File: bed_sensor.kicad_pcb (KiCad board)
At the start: 2 copper layers, 41 x 36 mm, 32 parts, among them J1 Conn_01x02, J2 Conn_01x06, J3 ISP, J4 Conn_01x02, Q1 2N2219, SW1 SW_SPST, U1 MIC5205-3.3, U2 MPU-9250, U5 CFAH0802D-YYH-JP, U6 ATMEGA328-AU, Y1 Crystal_GND2

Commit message: updated pcb layout
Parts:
- added C6: .1uF, Capacitor_SMD:C_0603_1608Metric, F.Cu at (147.4, 108.6)
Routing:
- net +3V3: track 144.0 -> 145.3 mm
- net GND: track 66.8 -> 68.2 mm, vias 12 -> 13
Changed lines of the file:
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@@
     (thickness 1.6)
     (drawings 12)
-    (tracks 435)
+    (tracks 442)
     (zones 0)
-    (modules 32)
+    (modules 33)
     (nets 32)
   )
@@
       (outputformat 1)
       (mirror false)
-      (drillshape 1)
+      (drillshape 0)
       (scaleselection 1)
-      (outputdirectory ""))
+      (outputdirectory ../../Downloads/bed_sensor_pcb/))
   )
   (net 0 "")
@@
     )
   )
+  (module Capacitor_SMD:C_0603_1608Metric (layer F.Cu)
+    (at 147.375001 108.63 180)
+    (descr "Capacitor SMD 0603 (1608 Metric), square (rectangular) end terminal, IPC_7351 nominal, (Body size source: http://www.tortai-tech.com/upload/download/2011102023233369053.pdf), generated with kicad-footprint-generator")
+    (tags capacitor)
+    (attr smd)
+    (fp_text reference C6 (at 0 -1.45 180) (layer F.SilkS)
+      (effects (font (size 1 1) (thickness 0.15)))
+    )
+    (fp_text value .1uF (at 0 1.45 180) (layer F.Fab)
+      (effects (font (size 1 1) (thickness 0.15)))
+    )
+    (fp_line (start -0.8 0.4) (end -0.8 -0.4) (layer F.Fab) (width 0.1))
+    (fp_line (start -0.8 -0.4) (end 0.8 -0.4) (layer F.Fab) (width 0.1))
+    (fp_line (start 0.8 -0.4) (end 0.8 0.4) (layer F.Fab) (width 0.1))
+    (fp_line (start 0.8 0.4) (end -0.8 0.4) (layer F.Fab) (width 0.1))
+    (fp_line (start -1.46 0.75) (end -1.46 -0.75) (layer F.CrtYd) (width 0.05))
+    (fp_line (start -1.46 -0.75) (end 1.46 -0.75) (layer F.CrtYd) (width 0.05))
+    (fp_line (start 1.46 -0.75) (end 1.46 0.75) (layer F.CrtYd) (width 0.05))
+    (fp_line (start 1.46 0.75) (end -1.46 0.75) (layer F.CrtYd) (width 0.05))
+    (fp_text user %R (at 0 0 180) (layer F.Fab)
+      (effects (font (size 0.4 0.4) (thickness 0.06)))
+    )
+    (pad 1 smd rect (at -0.8 0 180) (size 0.82 1) (layers F.Cu F.Paste F.Mask)
+      (net 2 GND))
+    (pad 2 smd rect (at 0.8 0 180) (size 0.82 1) (layers F.Cu F.Paste F.Mask)
+      (net 4 +3V3))
+    (model ${KISYS3DMOD}/Capacitor_SMD.3dshapes/C_0603_1608Metric.wrl
+      (at (xyz 0 0 0))
+      (scale (xyz 1 1 1))
+      (rotate (xyz 0 0 0))
+    )
+  )
   (gr_arc (start 117.749001 120.976) (end 116.225001 120.976) (angle -90) (layer Edge.Cuts) (width 0.15))
   (gr_arc (start 155.701001 120.976) (end 155.701001 122.5) (angle -90) (layer Edge.Cuts) (width 0.15))
@@
   (segment (start 142.693529 94.061472) (end 143.855001 92.9) (width 0.25) (layer F.Cu) (net 2))
   (segment (start 142.693529 94.458528) (end 142.693529 94.061472) (width 0.25) (layer F.Cu) (net 2))
+  (via (at 149.475001 108.59) (size 0.8) (drill 0.4) (layers F.Cu B.Cu) (net 2))
+  (segment (start 148.175001 108.63) (end 149.435001 108.63) (width 0.25) (layer F.Cu) (net 2))
+  (segment (start 149.435001 108.63) (end 149.475001 108.59) (width 0.25) (layer F.Cu) (net 2))
   (segment (start 150.559081 103.74808) (end 147.848001 101.037) (width 0.3) (layer F.Cu) (net 3) (status 30))
   (segment (start 150.559081 103.97816) (end 150.559081 103.74808) (width 0.3) (layer F.Cu) (net 3) (status 30))
@@
   (segment (start 145.485002 109.460001) (end 144.105001 109.460001) (width 0.2) (layer F.Cu) (net 4))
   (segment (start 145.485002 107.199999) (end 146.225001 106.46) (width 0.3) (layer F.Cu) (net 4))
-  (segment (start 145.485002 109.460001) (end 145.485002 107.199999) (width 0.3) (layer F.Cu) (net 4))
   (segment (start 145.685001 109.66) (end 145.485002 109.460001) (width 0.3) (layer F.Cu) (net 4))
   (segment (start 141.935001 109.98) (end 141.935001 111.8) (width 0.2) (layer F.Cu) (net 4))
@@
   (segment (start 145.393972 96.646029) (end 145.250224 96.646029) (width 0.3) (layer F.Cu) (net 4))
   (segment (start 142.236199 102.838802) (end 142.236199 99.660054) (width 0.3) (layer F.Cu) (net 4))
+  (segment (start 145.485002 109.009999) (end 145.865001 108.63) (width 0.3) (layer F.Cu) (net 4))
+  (segment (start 145.485002 109.1) (end 145.485002 109.009999) (width 0.3) (layer F.Cu) (net 4))
+  (segment (start 145.485002 109.460001) (end 145.485002 109.1) (width 0.3) (layer F.Cu) (net 4))
+  (segment (start 145.865001 108.63) (end 146.575001 108.63) (width 0.3) (layer F.Cu) (net 4))
+  (segment (start 145.485002 109.1) (end 145.485002 107.199999) (width 0.3) (layer F.Cu) (net 4))
   (segment (start 142.805001 109.91) (end 142.805001 110.9) (width 0.2) (layer F.Cu) (net 5))
   (segment (start 143.305001 111.4) (end 143.755001 111.4) (width 0.2) (layer F.Cu) (net 5))
@@
     (polygon
       (pts
-        (xy 111.975001 82.64) (xy 112.905001 135.17) (xy 161.375001 130.53) (xy 160.145001 82.35)
+        (xy 111.975001 82.64) (xy 112.905001 135.17) (xy 161.375001 130.53) (xy 159.515001 81.38)
       )
     )

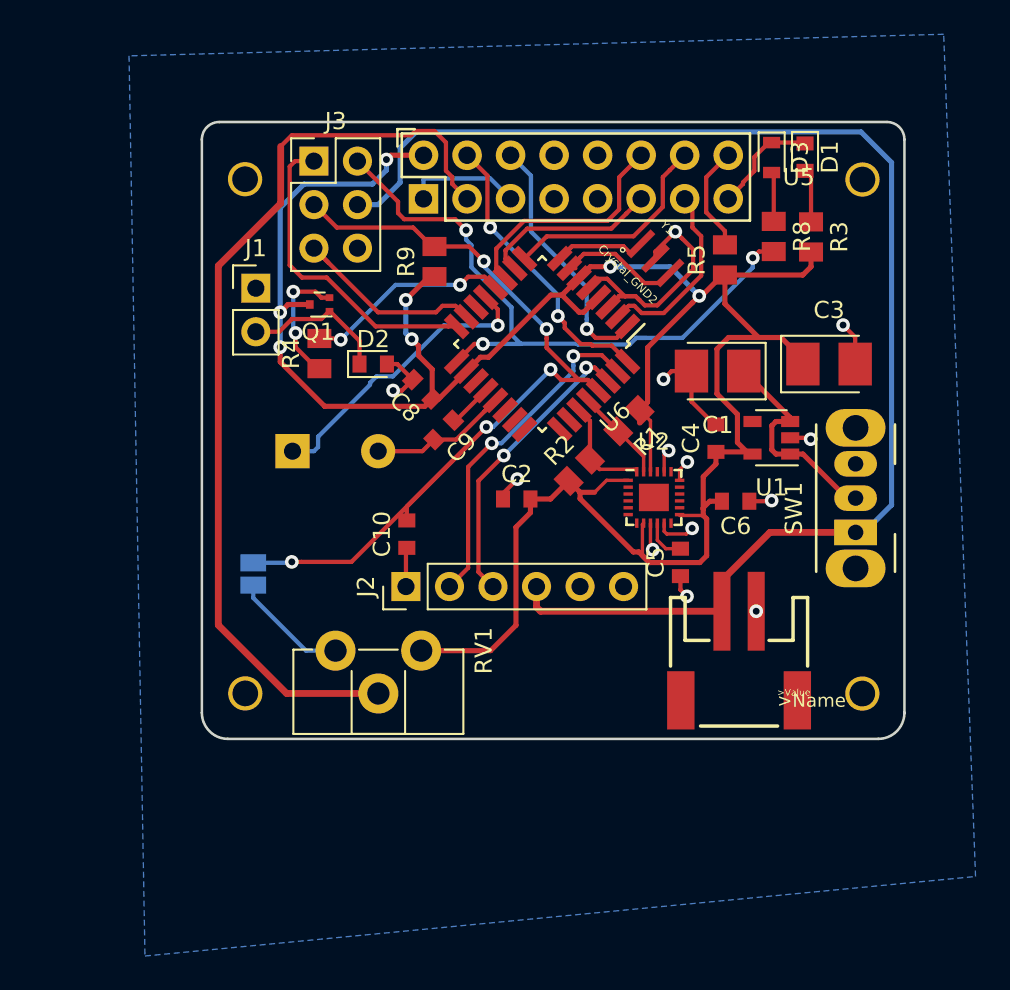
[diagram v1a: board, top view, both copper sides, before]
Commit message: corrected pinout for NHD display
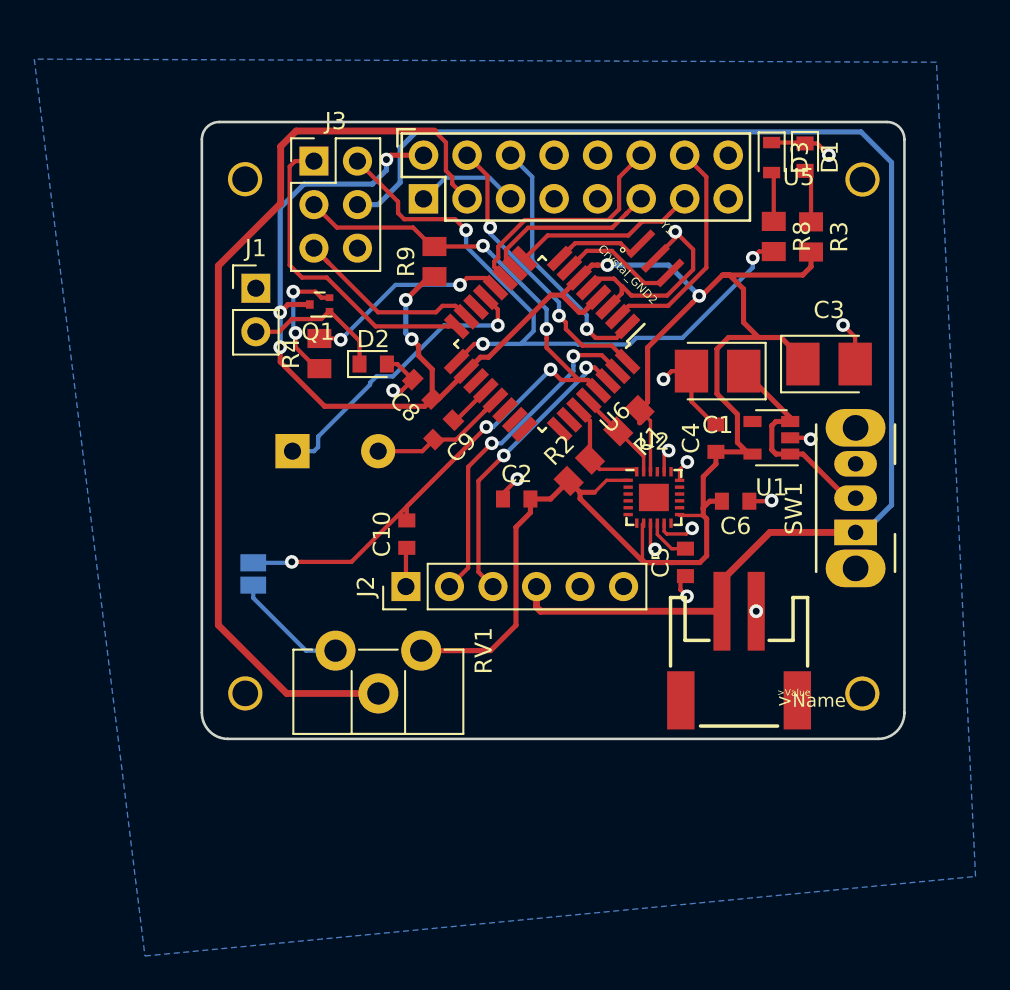
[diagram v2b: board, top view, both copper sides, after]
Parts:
- removed R5: 220, Resistor_SMD:R_0805_2012Metric
- moved C5 0.29 mm to (144.4, 112.2)
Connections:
- U1 pad 4: (no net) -> Net-(U1-Pad4)
- U2 pad 12: (no net) -> Net-(U2-Pad12)
- U2 pad 21: (no net) -> Net-(U2-Pad21)
- U2 pad 7: (no net) -> Net-(U2-Pad7)
- U5 pad 10: (no net) -> Net-(U5-Pad10)
- U5 pad 16: GND -> Net-(U5-Pad16)
- U5 pad 7: (no net) -> Net-(U5-Pad7)
- U5 pad 8: (no net) -> Net-(U5-Pad8)
- U5 pad 9: (no net) -> Net-(U5-Pad9)
- U6 pad 14: (no net) -> /Ardunio/D10
- U6 pad 19: (no net) -> /Ardunio/A6
- U6 pad 22: (no net) -> /Ardunio/A7
- U6 pad 23: (no net) -> /Ardunio/A0
- U6 pad 24: (no net) -> /Ardunio/A1
- U6 pad 25: (no net) -> /Ardunio/A2
- U6 pad 26: (no net) -> /Ardunio/A3
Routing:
- net Net-(U5-Pad15): track 6.22 -> 0.00 mm
- net GND: track 68.2 -> 63.8 mm, vias 13 -> 14
- net DB7: track 11.1 -> 13.4 mm
- net DB6: track 12.9 -> 10.8 mm
- net /Ardunio/RESET: track 52.0 -> 52.5 mm

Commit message: updated board
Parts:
- removed JP1: Jumper_NO_Small, Jumper:SolderJumper-2_P1.3mm_Open_Pad1.0x1.5mm
- removed U6: ATMEGA328-AU, Housings_QFP:TQFP-32_7x7mm_Pitch0.8mm
- added J5: DM3AT-SF-PEJM5, components:HRS_DM3AT-SF-PEJM5, B.Cu at (144.0, 104.0)
- added U3: ATMEGA328-AU, Package_QFP:TQFP-32_7x7mm_P0.8mm, F.Cu at (136.2, 99.5)
- moved J2 6.96 mm to (121.2, 113.7)
- moved C10 6.88 mm to (121.3, 110.7)
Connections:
- net /Ardunio/SCK renamed SCK
- J3 pad 1: /Ardunio/MISO -> MISO
- J3 pad 5: /Ardunio/MOSI -> MOSI
- U1 pad 4: Net-(U1-Pad4) -> (no net)
- U2 pad 12: Net-(U2-Pad12) -> (no net)
- U2 pad 21: Net-(U2-Pad21) -> (no net)
- U2 pad 7: Net-(U2-Pad7) -> (no net)
- U5 pad 10: Net-(U5-Pad10) -> (no net)
- U5 pad 15: Net-(U5-Pad15) -> (no net)
- U5 pad 16: Net-(U5-Pad16) -> (no net)
- U5 pad 7: Net-(U5-Pad7) -> (no net)
- U5 pad 8: Net-(U5-Pad8) -> (no net)
- U5 pad 9: Net-(U5-Pad9) -> (no net)
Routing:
- net MISO: track 0.00 -> 39.4 mm, vias 0 -> 3
- net MOSI: track 0.00 -> 26.3 mm, vias 0 -> 1
- net /Ardunio/MISO: track 18.5 -> 0.00 mm
- net CS: track 0.00 -> 13.8 mm, vias 0 -> 1
- net /Ardunio/MOSI: track 12.1 -> 0.00 mm
- net /Ardunio/RESET: track 52.5 -> 43.6 mm, vias 5 -> 4
- net +3V3: track 145.8 -> 154.6 mm, vias 7 -> 8
- net VCC: track 80.5 -> 87.3 mm, vias 0 -> 2
- net SCK: track 38.7 -> 44.1 mm
- net GND: track 63.8 -> 68.8 mm
- net /Ardunio/RX1: track 17.3 -> 21.3 mm
- net /Ardunio/TX0: track 19.8 -> 23.3 mm
- net Net-(D2-Pad1): track 8.61 -> 9.76 mm
- net Buzzer: track 17.4 -> 16.4 mm

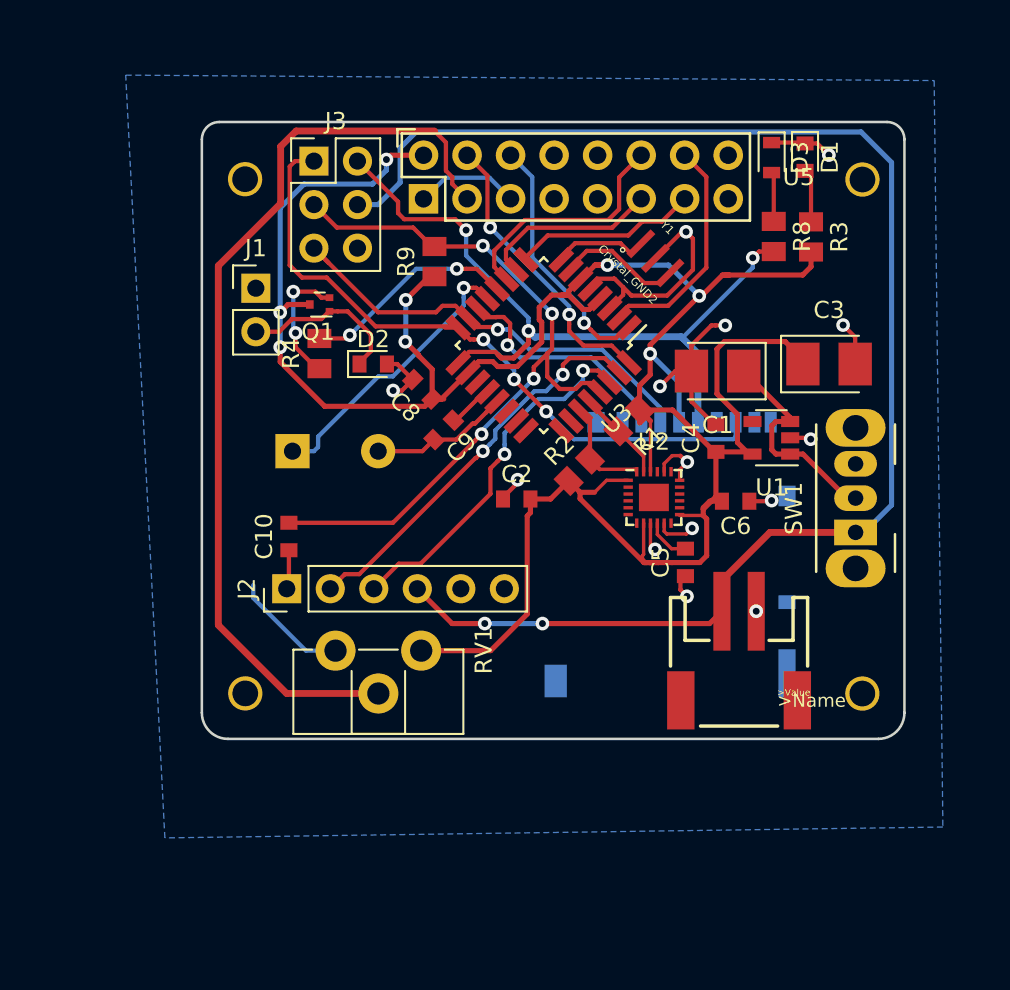
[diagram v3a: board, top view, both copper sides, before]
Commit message: updated design to accomidate screen better
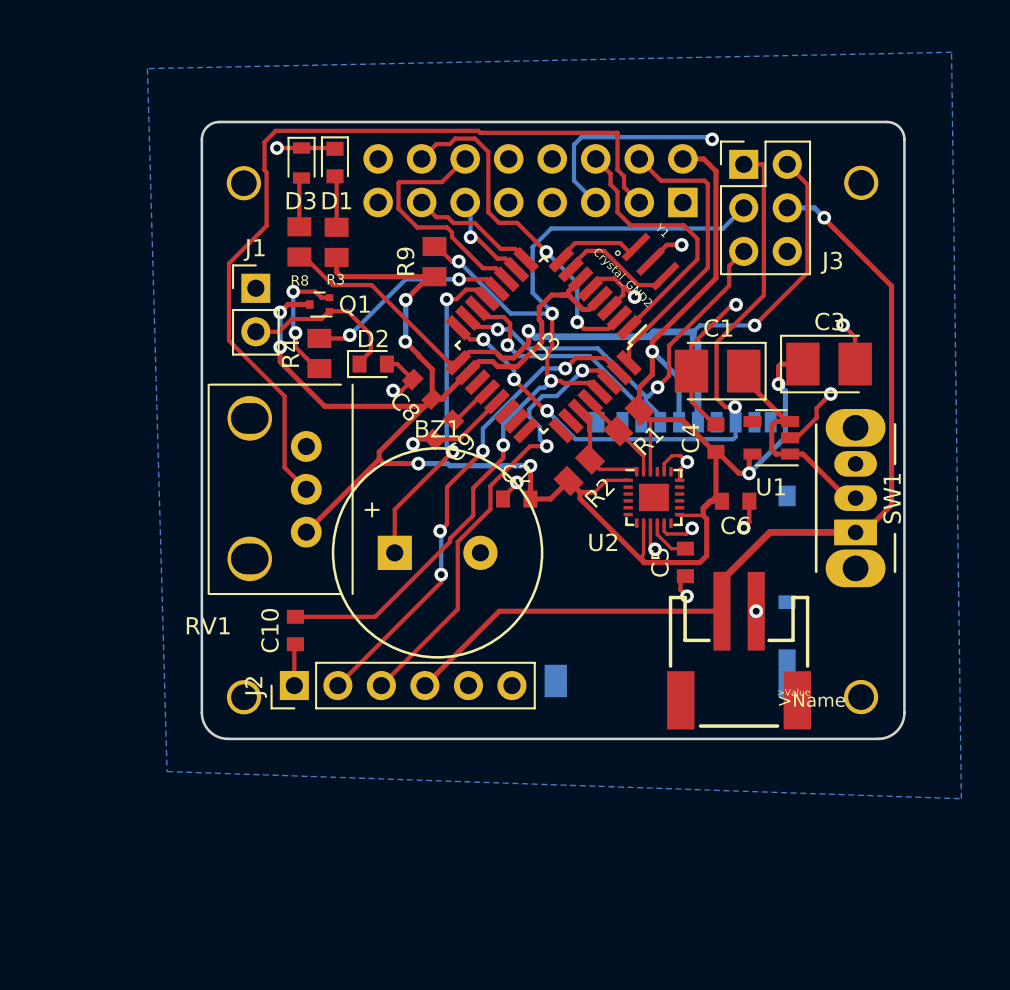
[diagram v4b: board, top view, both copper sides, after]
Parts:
- BZ1: moved to F.Cu
- RV1: footprint Potentiometers:Potentiometer_Trimmer_ACP_CA9h2.5_Vertical_Px2.5mm_Py5.0mm -> components:BI P090L-02F25BR10K
- U5: moved to B.Cu
- moved U5 36.1 mm to (118.7, 90.1), turned to 180 degrees
- moved R3 27.7 mm to (124.1, 93.5)
- moved R8 27.7 mm to (121.9, 93.5)
- moved D1 27.4 mm to (124.0, 88.9)
- moved D3 27.4 mm to (122.0, 88.9)
- moved J3 25.1 mm to (147.8, 89.0)
- moved RV1 11.3 mm to (119.0, 112.0), turned to 180 degrees
- moved BZ1 8.41 mm to (130.0, 111.6)
- moved J2 5.67 mm to (121.6, 119.4)
- moved C10 5.50 mm to (121.7, 116.2)
- moved Y1 0.34 mm to (142.4, 94.6)
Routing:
- net VCC: track 87.3 -> 53.9 mm, vias 2 -> 1
- net /Ardunio/RESET: track 43.6 -> 57.4 mm
- net +3V3: track 154.6 -> 143.4 mm, vias 8 -> 9
- net GND: track 68.8 -> 60.0 mm, vias 14 -> 16
- net DB7: track 13.4 -> 20.3 mm, vias 0 -> 2
- net Net-(RV1-Pad2): track 54.5 -> 48.6 mm
- net /Ardunio/RX1: track 21.3 -> 27.0 mm
- net /Ardunio/TX0: track 23.3 -> 28.5 mm, vias 2 -> 4
- net DB4: track 10.4 -> 5.61 mm, vias 0 -> 1
- net SCK: track 44.1 -> 48.1 mm, vias 3 -> 2
- net Buzzer: track 16.4 -> 19.8 mm, vias 1 -> 2
- net DB6: track 10.8 -> 7.48 mm
- net MOSI: track 26.3 -> 25.1 mm, vias 1 -> 2
- net Display_Enable: track 14.7 -> 15.8 mm, vias 1 -> 0
- net MISO: track 39.4 -> 38.6 mm, vias 3 -> 4
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
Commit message: working out missing sd card`
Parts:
- removed U3: ATMEGA328-AU, Package_QFP:TQFP-32_7x7mm_P0.8mm
- added U6: ATMEGA328-AU, Housings_QFP:TQFP-32_7x7mm_Pitch0.8mm, F.Cu at (136.2, 99.5)
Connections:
- J3 pad 1: MISO -> /Ardunio/MISO
- J3 pad 2: SCK -> VCC
- J3 pad 3: /Ardunio/RESET -> /Ardunio/SCK
- J3 pad 4: VCC -> /Ardunio/MOSI
- J3 pad 5: MOSI -> /Ardunio/RESET
- J5 pad 2: CS -> (no net)
- J5 pad 3: MOSI -> (no net)
- J5 pad 5: SCK -> (no net)
- J5 pad 7: MISO -> (no net)
- R8 pad 2: SCK -> /Ardunio/SCK
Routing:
- net SCK: track 48.1 -> 0.00 mm, vias 2 -> 0
- net MISO: track 38.6 -> 0.00 mm, vias 4 -> 0
- net /Ardunio/MISO: track 0.00 -> 38.6 mm, vias 0 -> 4
- net (no net): track 0.00 -> 32.9 mm, vias 0 -> 2
- net CS: track 13.8 -> 0.00 mm, vias 1 -> 0
- net /Ardunio/SCK: track 0.00 -> 12.0 mm
- net /Ardunio/RESET: track 57.4 -> 55.7 mm
